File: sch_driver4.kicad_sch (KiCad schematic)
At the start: 16 parts, among them Q4 PSMN4R0-30YLDX, U14 TS5A3159ADCK, U2 ADA4099-2xR, U24 OPA333

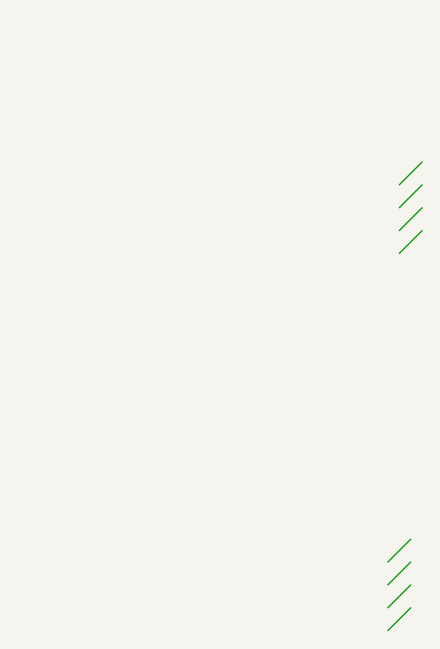
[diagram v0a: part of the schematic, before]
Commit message: Finished schematic refactor to six A-sheets. Updated PCB.
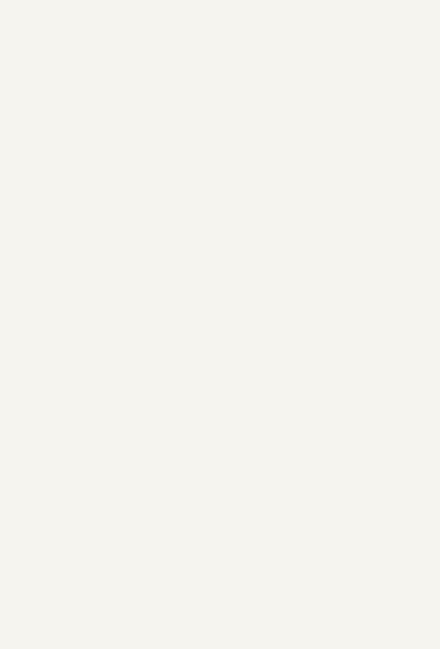
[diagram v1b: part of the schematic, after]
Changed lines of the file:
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@@
 	(title_block
 		(title "PBM Driver 4 V2")
-		(date "23-DEC-2025")
+		(date "24-DEC-2025")
 		(rev "A")
 		(comment 1 "Part Number: PCB104 Rev A")
@@
 		(color 0 0 0 0)
 	)
-	(bus_entry
-		(at 389.89 226.06)
-		(size -2.54 2.54)
-		(stroke
-			(width 0)
-			(type default)
-		)
-	)
-	(bus_entry
-		(at 389.89 223.52)
-		(size -2.54 2.54)
-		(stroke
-			(width 0)
-			(type default)
-		)
-	)
-	(bus_entry
-		(at 391.16 181.61)
-		(size -2.54 2.54)
-		(stroke
-			(width 0)
-			(type default)
-		)
-	)
-	(bus_entry
-		(at 391.16 179.07)
-		(size -2.54 2.54)
-		(stroke
-			(width 0)
-			(type default)
-		)
-	)
-	(bus_entry
-		(at 389.89 220.98)
-		(size -2.54 2.54)
-		(stroke
-			(width 0)
-			(type default)
-		)
-	)
-	(bus_entry
-		(at 391.16 184.15)
-		(size -2.54 2.54)
-		(stroke
-			(width 0)
-			(type default)
-		)
-	)
-	(bus_entry
-		(at 391.16 176.53)
-		(size -2.54 2.54)
-		(stroke
-			(width 0)
-			(type default)
-		)
-	)
-	(bus_entry
-		(at 389.89 218.44)
-		(size -2.54 2.54)
-		(stroke
-			(width 0)
-			(type default)
-		)
-	)
 	(wire

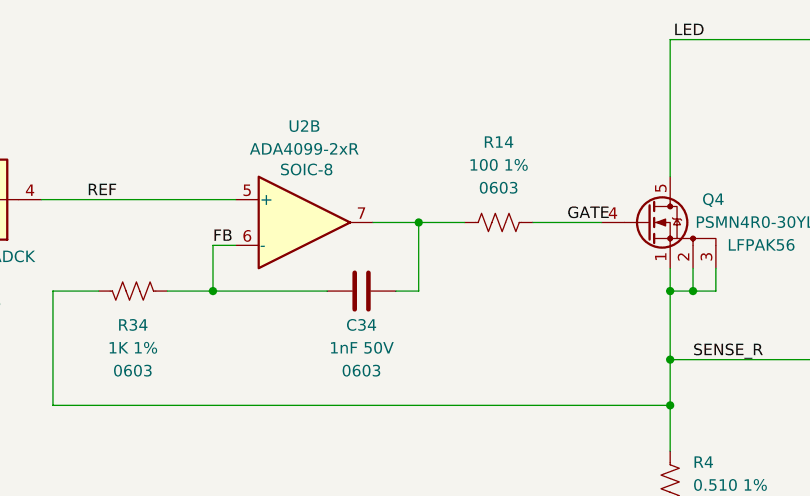
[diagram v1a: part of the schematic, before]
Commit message: Routing WIP. Prep to look at SOT-23 op amps for U1 and U2. Added convenience link to Git Bash.
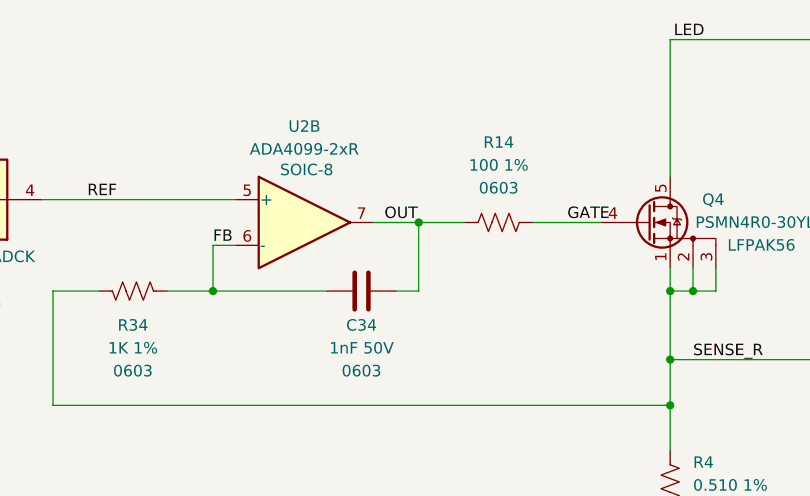
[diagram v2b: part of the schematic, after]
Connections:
- net OUT: now reaches C34.2, R14.1, U2.7
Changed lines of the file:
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@@
+		)
+	)
+	(label "OUT"
+		(at 110.49 53.34 0)
+		(effects
+			(font
+				(size 1.27 1.27)
+			)
+			(justify left bottom)
 		)
 	)

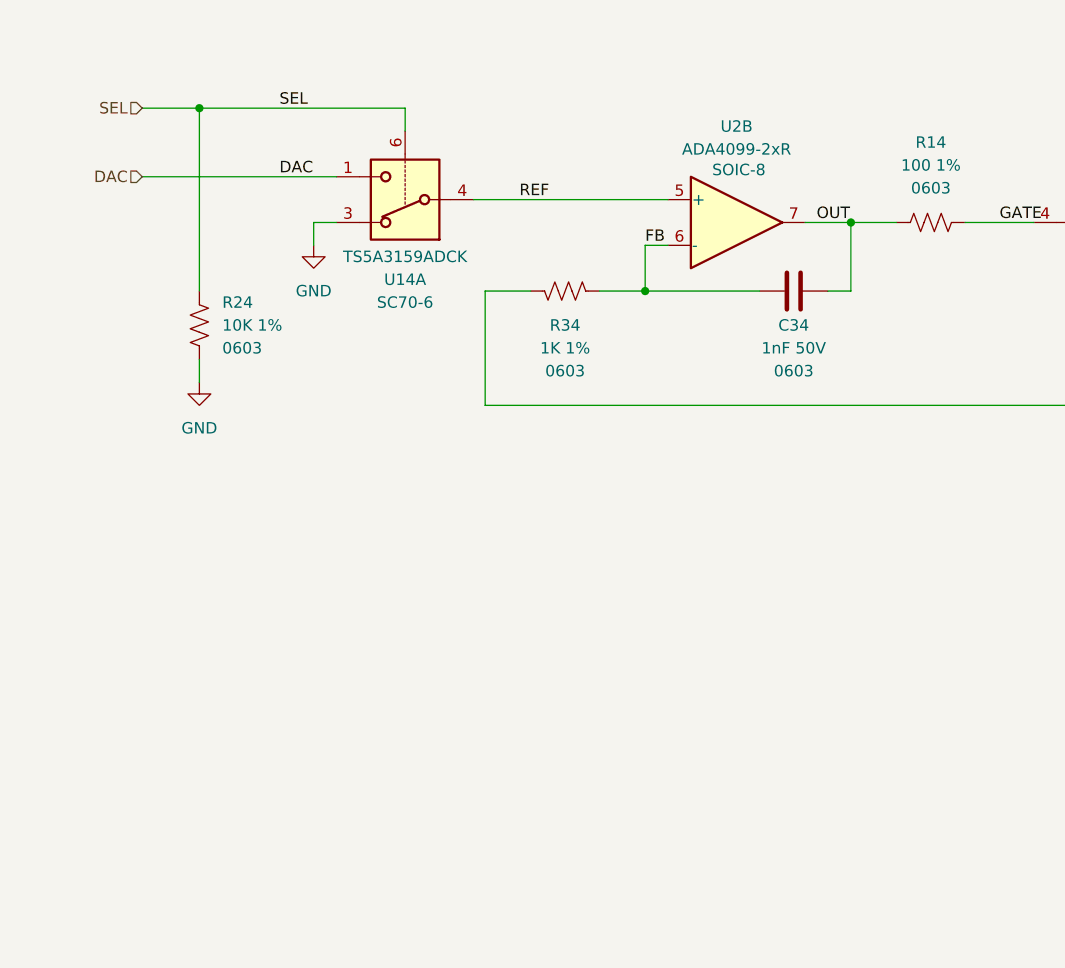
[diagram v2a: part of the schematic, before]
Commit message: Routing WIP with SOT-23 op amps
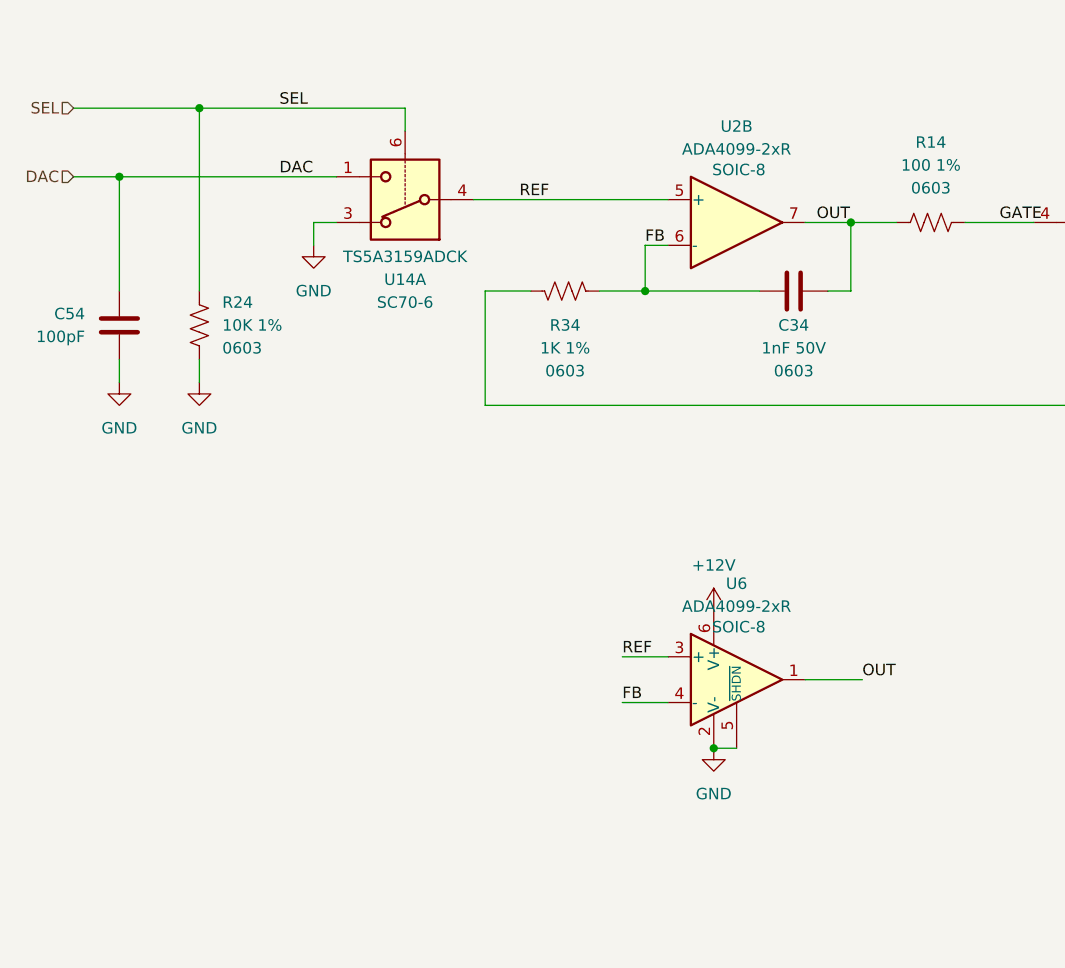
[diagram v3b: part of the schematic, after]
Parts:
- added C54: 100pF, $Local:C_0603_1608Metric, symbol $Local:C
- added U6: ADA4099-2xR, Package_TO_SOT_SMD:TSOT-23-6, symbol Amplifier_Operational:ADA4099-1xUJ
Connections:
- net DAC: now also C54.1
- net FB: now also U6.4 (-)
- net GND: now also C54.2, U6.2 (V-), U6.5 (~{SHDN})
- net OUT: now also U6.1
- net REF: now also U6.3 (+)
- new net +12V: U6.6 (V+)

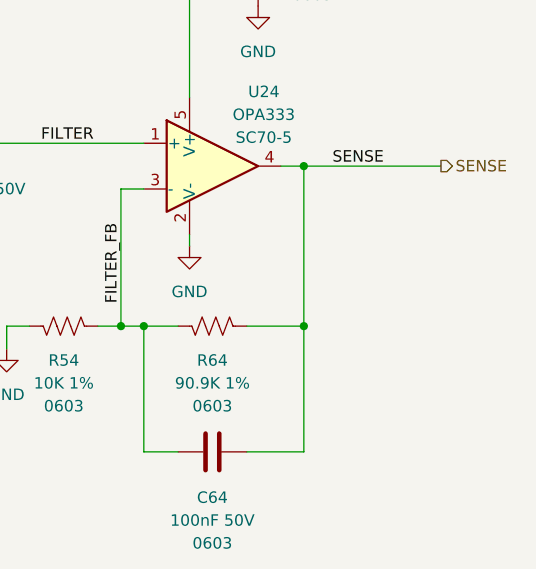
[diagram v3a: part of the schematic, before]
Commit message: Added pull-downs to output of Sense filter op amps
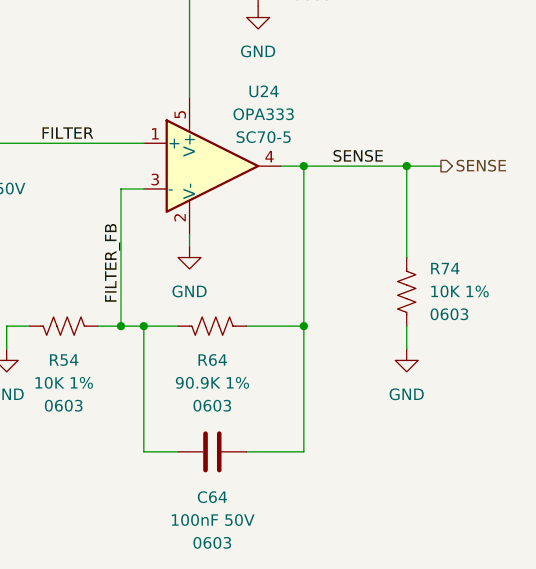
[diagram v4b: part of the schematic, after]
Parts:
- added R74: 10K 1%, $Local:R_0603_1608Metric, symbol $Local:R_0603_10K
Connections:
- net GND: now also R74.2
- net SENSE: now also R74.1
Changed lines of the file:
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@@
+	)
+	(junction
+		(at 237.49 71.12)
+		(diameter 0)
+		(color 0 0 0 0)
 	)
 	(junction
@@
 	(wire
 		(pts
+			(xy 237.49 71.12) (xy 241.3 71.12)
+		)
+		(stroke
+			(width 0)
+			(type default)
+		)
+	)
+	(wire
+		(pts
 			(xy 118.11 177.8) (xy 95.25 177.8)
 		)
@@
 	(wire
 		(pts
+			(xy 237.49 71.12) (xy 237.49 81.28)
+		)
+		(stroke
+			(width 0)
+			(type default)
+		)
+	)
+	(wire
+		(pts
 			(xy 205.74 88.9) (xy 208.28 88.9)
 		)
@@
 	(wire
 		(pts
+			(xy 237.49 88.9) (xy 237.49 91.44)
+		)
+		(stroke
+			(width 0)
+			(type default)
+		)
+	)
+	(wire
+		(pts
 			(xy 99.06 111.76) (xy 101.6 111.76)
 		)
@@
 	(wire
 		(pts
-			(xy 226.06 71.12) (xy 241.3 71.12)
+			(xy 226.06 71.12) (xy 237.49 71.12)
 		)
 		(stroke
@@
 	)
 	(symbol
+		(lib_id "$Local:R_0603_10K")
+		(at 237.49 85.09 0)
+		(unit 1)
+		(exclude_from_sim no)
+		(in_bom yes)
+		(on_board yes)
+		(dnp no)
+		(fields_autoplaced yes)
+		(property "Reference" "R74"
+			(at 240.03 82.5499 0)
+			(effects
+				(font
+					(size 1.27 1.27)
+				)
+				(justify left)
+			)
+		)
+		(property "Value" "10K 1%"
+			(at 240.03 85.0899 0)
+			(effects
+				(font
+					(size 1.27 1.27)
+				)
+				(justify left)
+			)
+		)
+		(property "Footprint" "$Local:R_0603_1608Metric"
+			(at 238.506 85.344 90)
+			(effects
+				(font
+					(size 1.27 1.27)
+				)
+				(hide yes)
+			)
+		)
+		(property "Datasheet" "~"
+			(at 237.49 85.09 0)
+			(effects
+				(font
+					(size 1.27 1.27)
+				)
+				(hide yes)
+			)
+		)
+		(property "Description" "RES SMD 10K OHM 1% 1/10W 0603"
+			(at 237.49 85.09 0)
+			(effects
+				(font
+					(size 1.27 1.27)
+				)
+				(hide yes)
+			)
+		)
+		(property "Size" "0603"
+			(at 240.03 87.6299 0)
+			(effects
+				(font
+					(size 1.27 1.27)
+				)
+				(justify left)
+			)
+		)
+		(property "PN" ""
+			(at 237.49 85.09 0)
+			(effects
+				(font
+					(size 1.27 1.27)
+				)
+				(hide yes)
+			)
+		)
+		(pin "1"
+		)
+		(pin "2"
+		)
+		(instances
+			(project "pbm_driver4_v2"
+				(path "/04797749-7aaf-42f7-a5f4-0b9aeb0ad7be/0d8fba0c-1337-4987-b588-0137eadfd0ea"
+					(reference "R74")
+					(unit 1)
+				)
+			)
+		)
+	)
+	(symbol
 		(lib_id "$Local:C")
 		(at 33.02 64.77 0)
@@
 					(unit 1)
 				)
+			)
+		)
+	)
+	(symbol
+		(lib_id "$Local:GND")
+		(at 237.49 91.44 0)
+		(unit 1)
+		(exclude_from_sim no)
+		(in_bom yes)
+		(on_board yes)
+		(dnp no)
+		(fields_autoplaced yes)
+		(property "Reference" "#PWR037"
+			(at 237.49 97.79 0)
+			(effects
+				(font
+					(size 1.27 1.27)
+				)
+				(hide yes)
+			)
+		)
+		(property "Value" "GND"
+			(at 237.49 96.52 0)
+			(effects
+				(font
+					(size 1.27 1.27)
+				)
+			)
+		)
+		(property "Footprint" ""
+			(at 237.49 91.44 0)
+			(effects
+				(font
+					(size 1.27 1.27)
+				)
+				(hide yes)
+			)
+		)
+		(property "Datasheet" ""
+			(at 237.49 91.44 0)
+			(effects
+				(font
+					(size 1.27 1.27)
+				)
+				(hide yes)
+			)
+		)
+		(property "Description" "Power symbol creates a global label with name \"GND\" , ground"
+			(at 237.49 91.44 0)
+			(effects
+				(font
+					(size 1.27 1.27)
+				)
+				(hide yes)
+			)
+		)
+		(pin "1"
+		)
+		(instances
+			(project "pbm_driver4_v2"
+				(path "/04797749-7aaf-42f7-a5f4-0b9aeb0ad7be/0d8fba0c-1337-4987-b588-0137eadfd0ea"
+					(reference "#PWR037")
+					(unit 1)
+				)
